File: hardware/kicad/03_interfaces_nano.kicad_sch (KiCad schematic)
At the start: 44 parts, among them J1001 NANO P1 2x13, J1002 NANO P2 2x13, J1003 DEBUG HEADER, J701 NANO DSI 15P, J702 DISPLAYMAN LCD 40P, J801 GT9271 TOUCH 8P, Q801 MMBT3904, U701 TPD6E05U06RVZR, U801 TLV75533PDBVR, U802 TMUX1574PWR, U803 TPD4E05U06DQAR

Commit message: Simplify power architecture to single 12V input
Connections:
- net VEH_PGOOD renamed SYS24_PGOOD
- net VIN_PROT_24V renamed SYS_24V
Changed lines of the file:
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@@
 	(title_block
 		(title "Interfaces & Nano")
-		(date "2026-09-18")
-		(rev "Phase 2 / audit correction v0.3")
+		(date "2026-09-19")
+		(rev "Phase 2 / single-source v0.4")
 		(company "ESP32-P4 Displayman Development Daughterboard")
 		(comment 1 "© 2026 Sy Aryeh")
@@
 		)
 	)
-	(global_label "VIN_PROT_24V"
+	(global_label "SYS_24V"
 		(shape bidirectional)
 		(at 673.1 48.26 0)
@@
 		)
 	)
-	(global_label "VEH_PGOOD"
+	(global_label "SYS24_PGOOD"
 		(shape bidirectional)
 		(at 730.25 302.26 0)

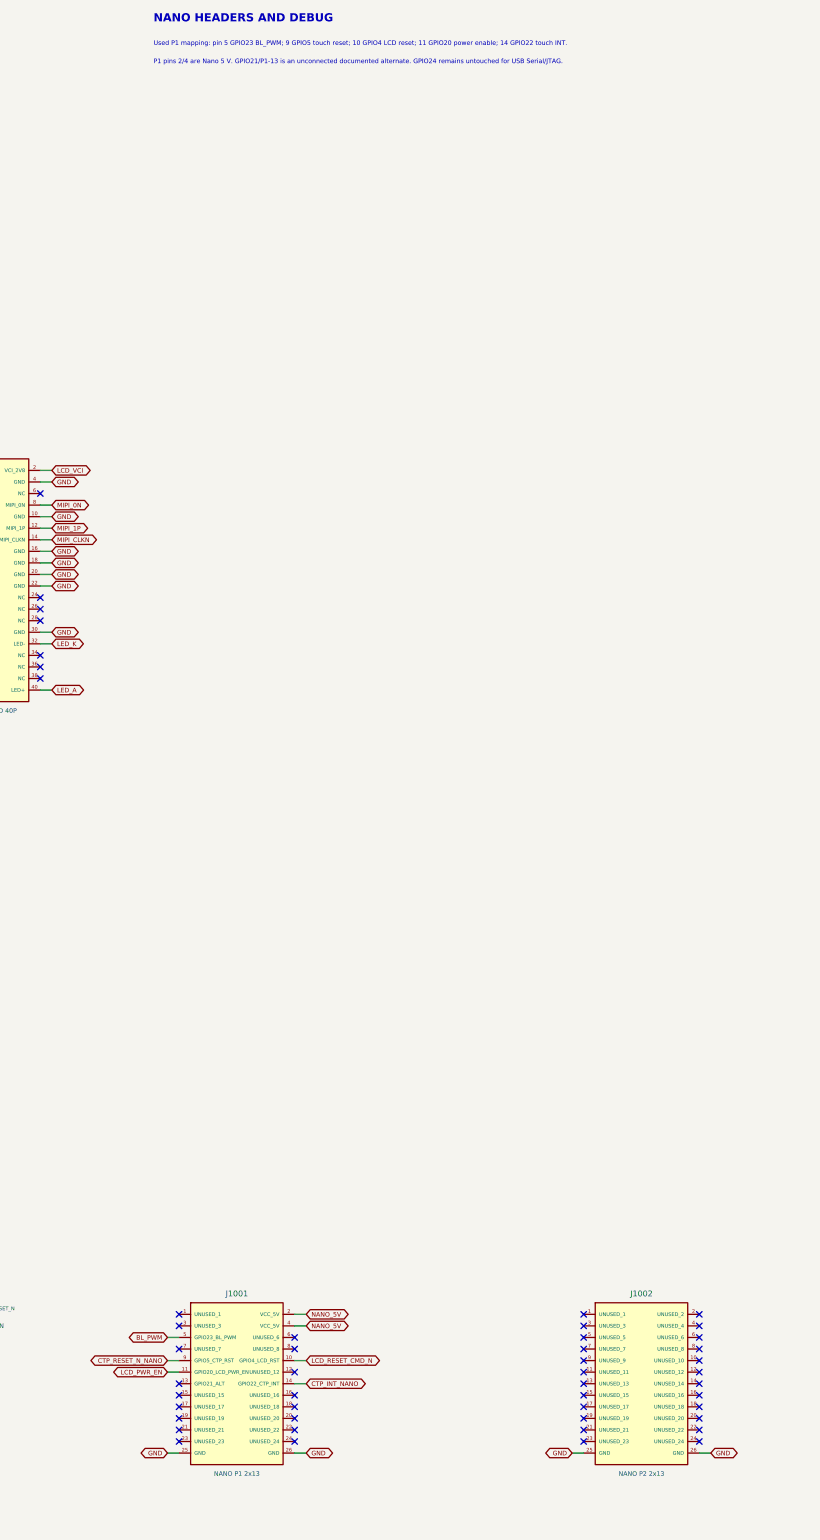
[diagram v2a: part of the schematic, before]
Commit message: Correct Nano interface and document floorplan study
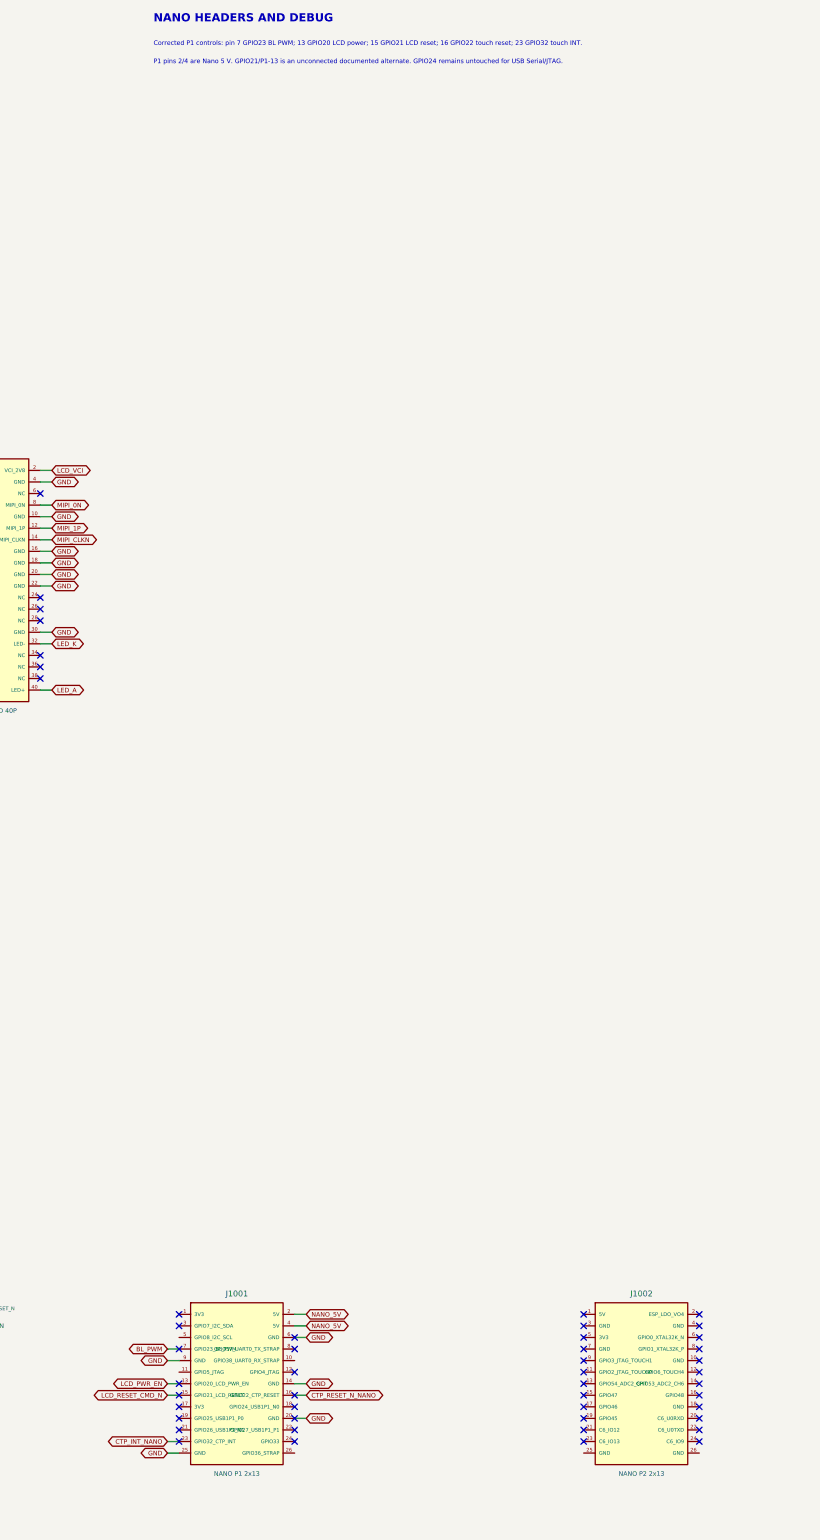
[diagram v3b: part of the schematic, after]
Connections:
- net BL_PWM: now also J1001.7 (GPIO23_BL_PWM); no longer J1001.5 (GPIO23_BL_PWM)
- net CTP_INT_NANO: now also J1001.23 (GPIO32_CTP_INT); no longer J1001.14 (GPIO22_CTP_INT)
- net CTP_RESET_N_NANO: now also J1001.16 (GPIO22_CTP_RESET); no longer J1001.9 (GPIO5_CTP_RST)
- net GND: now also J1001.14 (GND), J1001.20 (GND), J1001.6 (GND), J1001.9 (GND); no longer J1001.26 (GND), J1002.25 (GND), J1002.26 (GND)
- net LCD_PWR_EN: now also J1001.13 (GPIO20_LCD_PWR_EN); no longer J1001.11 (GPIO20_LCD_PWR_EN)
- net LCD_RESET_CMD_N: now also J1001.15 (GPIO21_LCD_RESET); no longer J1001.10 (GPIO4_LCD_RST)
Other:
- note added: "Corrected P1 controls: pin 7 GPIO23 BL PWM; 13 GPIO20 LCD power; 15 GPIO21 LCD reset; 16 GPIO22 touch reset; 23 GPIO32 touch INT."
- note removed: "Used P1 mapping: pin 5 GPIO23 BL_PWM; 9 GPIO5 touch reset; 10 GPIO4 LCD reset; 11 GPIO20 power enable; 14 GPIO22 touch INT."
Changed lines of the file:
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@@
 		(comment 3 "REV1 development hardware")
 	)
-	(text "Used P1 mapping: pin 5 GPIO23 BL_PWM; 9 GPIO5 touch reset; 10 GPIO4 LCD reset; 11 GPIO20 power enable; 14 GPIO22 touch INT."
+	(text "Corrected P1 controls: pin 7 GPIO23 BL PWM; 13 GPIO20 LCD power; 15 GPIO21 LCD reset; 16 GPIO22 touch reset; 23 GPIO32 touch INT."
 		(exclude_from_sim no)
 		(at 432.54 35.16 0)
@@
 			)
 		)
-		(property "Description" "Nano stack header; only source-confirmed used pins assigned"
+		(property "Description" "Waveshare Nano P1 header; complete host pin functions shown"
 			(at 450.85 328.93 0)
 			(hide yes)
@@
 			)
 		)
-		(property "Description" "Nano stack header; no signals required by this daughterboard"
+		(property "Description" "Waveshare Nano P2 header; electrically unused by daughterboard"
 			(at 539.75 328.93 0)
 			(hide yes)
@@
 	(wire
 		(pts
-			(xy 438.15 318.77) (xy 435.61 318.77)
+			(xy 438.15 321.31) (xy 435.61 321.31)
 		)
 		(stroke
@@
 	(global_label "BL_PWM"
 		(shape bidirectional)
-		(at 435.61 318.77 180)
+		(at 435.61 321.31 180)
 		(fields_autoplaced yes)
 		(effects
@@
 		)
 		(property "Intersheetrefs" "${INTERSHEET_REFS}"
-			(at 434.34 318.77 180)
+			(at 434.34 321.31 180)
 			(hide yes)
 			(show_name no)
@@
 	(wire
 		(pts
-			(xy 438.15 323.85) (xy 435.61 323.85)
+			(xy 438.15 328.93) (xy 435.61 328.93)
 		)
 		(stroke
@@
 		)
 	)
-	(global_label "CTP_RESET_N_NANO"
+	(global_label "LCD_PWR_EN"
 		(shape bidirectional)
-		(at 435.61 323.85 180)
+		(at 435.61 328.93 180)
 		(fields_autoplaced yes)
 		(effects
@@
 		)
 		(property "Intersheetrefs" "${INTERSHEET_REFS}"
-			(at 434.34 323.85 180)
+			(at 434.34 328.93 180)
 			(hide yes)
 			(show_name no)
@@
 	(wire
 		(pts
-			(xy 463.55 323.85) (xy 466.09 323.85)
+			(xy 438.15 331.47) (xy 435.61 331.47)
 		)
 		(stroke
@@
 	(global_label "LCD_RESET_CMD_N"
 		(shape bidirectional)
-		(at 466.09 323.85 0)
+		(at 435.61 331.47 180)
+		(fields_autoplaced yes)
+		(effects
+			(font
+				(size 1 1)
+			)
+			(justify right)
+		)
+		(property "Intersheetrefs" "${INTERSHEET_REFS}"
+			(at 434.34 331.47 180)
+			(hide yes)
+			(show_name no)
+			(do_not_autoplace no)
+			(effects
+				(font
+					(size 1 1)
+				)
+				(justify right)
+			)
+		)
+	)
+	(wire
+		(pts
+			(xy 463.55 331.47) (xy 466.09 331.47)
+		)
+		(stroke
+			(width 0)
+			(type default)
+		)
+	)
+	(global_label "CTP_RESET_N_NANO"
+		(shape bidirectional)
+		(at 466.09 331.47 0)
 		(fields_autoplaced yes)
 		(effects
@@
 		)
 		(property "Intersheetrefs" "${INTERSHEET_REFS}"
-			(at 467.36 323.85 0)
+			(at 467.36 331.47 0)
 			(hide yes)
 			(show_name no)
@@
 	(wire
 		(pts
-			(xy 438.15 326.39) (xy 435.61 326.39)
+			(xy 438.15 341.63) (xy 435.61 341.63)
 		)
 		(stroke
@@
 		)
 	)
-	(global_label "LCD_PWR_EN"
+	(global_label "CTP_INT_NANO"
 		(shape bidirectional)
-		(at 435.61 326.39 180)
+		(at 435.61 341.63 180)
 		(fields_autoplaced yes)
 		(effects
@@
 		)
 		(property "Intersheetrefs" "${INTERSHEET_REFS}"
-			(at 434.34 326.39 180)
+			(at 434.34 341.63 180)
 			(hide yes)
 			(show_name no)
@@
 	(wire
 		(pts
-			(xy 463.55 328.93) (xy 466.09 328.93)
+			(xy 438.15 344.17) (xy 435.61 344.17)
 		)
 		(stroke
@@
 		)
 	)
-	(global_label "CTP_INT_NANO"
+	(global_label "GND"
 		(shape bidirectional)
-		(at 466.09 328.93 0)
+		(at 435.61 344.17 180)
+		(fields_autoplaced yes)
+		(effects
+			(font
+				(size 1 1)
+			)
+			(justify right)
+		)
+		(property "Intersheetrefs" "${INTERSHEET_REFS}"
+			(at 434.34 344.17 180)
+			(hide yes)
+			(show_name no)
+			(do_not_autoplace no)
+			(effects
+				(font
+					(size 1 1)
+				)
+				(justify right)
+			)
+		)
+	)
+	(wire
+		(pts
+			(xy 463.55 318.77) (xy 466.09 318.77)
+		)
+		(stroke
+			(width 0)
+			(type default)
+		)
+	)
+	(global_label "GND"
+		(shape bidirectional)
+		(at 466.09 318.77 0)
 		(fields_autoplaced yes)
 		(effects
@@
 		)
 		(property "Intersheetrefs" "${INTERSHEET_REFS}"
-			(at 467.36 328.93 0)
+			(at 467.36 318.77 0)
 			(hide yes)
 			(show_name no)
@@
 	(wire
 		(pts
-			(xy 438.15 344.17) (xy 435.61 344.17)
+			(xy 438.15 323.85) (xy 435.61 323.85)
 		)
 		(stroke
@@
 	(global_label "GND"
 		(shape bidirectional)
-		(at 435.61 344.17 180)
+		(at 435.61 323.85 180)
 		(fields_autoplaced yes)
 		(effects
@@
 		)
 		(property "Intersheetrefs" "${INTERSHEET_REFS}"
-			(at 434.34 344.17 180)
+			(at 434.34 323.85 180)
 			(hide yes)
 			(show_name no)
@@
 	(wire
 		(pts
-			(xy 463.55 344.17) (xy 466.09 344.17)
+			(xy 463.55 328.93) (xy 466.09 328.93)
 		)
 		(stroke
@@
 	(global_label "GND"
 		(shape bidirectional)
-		(at 466.09 344.17 0)
+		(at 466.09 328.93 0)
 		(fields_autoplaced yes)
 		(effects
@@
 		)
 		(property "Intersheetrefs" "${INTERSHEET_REFS}"
-			(at 467.36 344.17 0)
+			(at 467.36 328.93 0)
+			(hide yes)
+			(show_name no)
+			(do_not_autoplace no)
+			(effects
+				(font
+					(size 1 1)
+				)
+				(justify left)
+			)
+		)
+	)
+	(wire
+		(pts
+			(xy 463.55 336.55) (xy 466.09 336.55)
+		)
+		(stroke
+			(width 0)
+			(type default)
+		)
+	)
+	(global_label "GND"
+		(shape bidirectional)
+		(at 466.09 336.55 0)
+		(fields_autoplaced yes)
+		(effects
+			(font
+				(size 1 1)
+			)
+			(justify left)
+		)
+		(property "Intersheetrefs" "${INTERSHEET_REFS}"
+			(at 467.36 336.55 0)
 			(hide yes)
 			(show_name no)
@@
 			(hide yes)
 			(show_name no)
-			(do_not_autoplace no)
-			(effects
-				(font
-					(size 1 1)
-				)
-				(justify left)
-			)
-		)
-	)
-	(wire
-		(pts
-			(xy 527.05 344.17) (xy 524.51 344.17)
-		)
-		(stroke
-			(width 0)
-			(type default)
-		)
-	)
-	(global_label "GND"
-		(shape bidirectional)
-		(at 524.51 344.17 180)
-		(fields_autoplaced yes)
-		(effects
-			(font
-				(size 1 1)
-			)
-			(justify right)
-		)
-		(property "Intersheetrefs" "${INTERSHEET_REFS}"
-			(at 523.24 344.17 180)
-			(hide yes)
-			(show_name no)
-			(do_not_autoplace no)
-			(effects
-				(font
-					(size 1 1)
-				)
-				(justify right)
-			)
-		)
-	)
-	(wire
-		(pts
-			(xy 552.45 344.17) (xy 554.99 344.17)
-		)
-		(stroke
-			(width 0)
-			(type default)
-		)
-	)
-	(global_label "GND"
-		(shape bidirectional)
-		(at 554.99 344.17 0)
-		(fields_autoplaced yes)
-		(effects
-			(font
-				(size 1 1)
-			)
-			(justify left)
-		)
-		(property "Intersheetrefs" "${INTERSHEET_REFS}"
-			(at 556.26 344.17 0)
-			(hide yes)
-			(show_name no)

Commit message: Validate SSQ stack and add preliminary PCB placement
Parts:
- J1001: value NANO P1 2x13 -> SSQ-113-01-G-D; footprint Connector_PinSocket_2.54mm:PinSocket_2x13_P2.54mm_Vertical -> Phase2:Samtec_SSQ-113-01-G-D_BottomMount; MPN SSW-113-02-G-D -> SSQ-113-01-G-D
- J1002: value NANO P2 2x13 -> SSQ-113-01-G-D; footprint Connector_PinSocket_2.54mm:PinSocket_2x13_P2.54mm_Vertical -> Phase2:Samtec_SSQ-113-01-G-D_BottomMount; MPN SSW-113-02-G-D -> SSQ-113-01-G-D
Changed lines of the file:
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@@
 			)
 		)
-		(property "Value" "NANO P1 2x13"
+		(property "Value" "SSQ-113-01-G-D"
 			(at 450.85 348.71 0)
 			(show_name no)
@@
 			)
 		)
-		(property "Footprint" "Connector_PinSocket_2.54mm:PinSocket_2x13_P2.54mm_Vertical"
+		(property "Footprint" "Phase2:Samtec_SSQ-113-01-G-D_BottomMount"
 			(at 450.85 328.93 0)
 			(hide yes)
@@
 			)
 		)
-		(property "Datasheet" ""
+		(property "Datasheet" "https://www.samtec.com/products/ssq-113-01-g-d"
 			(at 450.85 328.93 0)
 			(hide yes)
@@
 			)
 		)
-		(property "Description" "Waveshare Nano P1 header; complete host pin functions shown"
+		(property "Description" "Samtec 2x13 2.54 mm vertical socket on Waveshare Nano P1; complete host pin functions shown"
 			(at 450.85 328.93 0)
 			(hide yes)
@@
 			)
 		)
-		(property "MPN" "SSW-113-02-G-D"
+		(property "MPN" "SSQ-113-01-G-D"
 			(at 450.85 328.93 0)
 			(hide yes)
@@
 			)
 		)
-		(property "Value" "NANO P2 2x13"
+		(property "Value" "SSQ-113-01-G-D"
 			(at 539.75 348.71 0)
 			(show_name no)
@@
 			)
 		)
-		(property "Footprint" "Connector_PinSocket_2.54mm:PinSocket_2x13_P2.54mm_Vertical"
+		(property "Footprint" "Phase2:Samtec_SSQ-113-01-G-D_BottomMount"
 			(at 539.75 328.93 0)
 			(hide yes)
@@
 			)
 		)
-		(property "Datasheet" ""
+		(property "Datasheet" "https://www.samtec.com/products/ssq-113-01-g-d"
 			(at 539.75 328.93 0)
 			(hide yes)
@@
 			)
 		)
-		(property "Description" "Waveshare Nano P2 header; electrically unused by daughterboard"
+		(property "Description" "Samtec 2x13 2.54 mm vertical socket on Waveshare Nano P2; electrically unused alignment interface"
 			(at 539.75 328.93 0)
 			(hide yes)
@@
 			)
 		)
-		(property "MPN" "SSW-113-02-G-D"
+		(property "MPN" "SSQ-113-01-G-D"
 			(at 539.75 328.93 0)
 			(hide yes)
